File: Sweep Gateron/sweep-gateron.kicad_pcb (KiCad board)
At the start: 2 copper layers, 229.5 x 95.2 mm, 61 parts, among them J1 AudioJack4dpb, J2 AudioJack4dpb, SW10 SW_Push, SW11 SW_Push, SW11_r1 SW_Push, SW12 SW_Push, SW12_r1 SW_Push, SW13_r1 SW_Push, SW14 SW_Push, SW15 SW_Push, SW15_r1 SW_Push, SW16 SW_Push, SW16_r1 SW_Push, SW17 SW_Push, SW17_r1 SW_Push, SW18 SW_Push, SW18_r1 SW_Push, SW2 SW_Push, SW2 SW_SPDT, SW20 SW_Push, SW21 SW_Push, SW2_r1 SW_Push, SW3 SW_Push, SW3_r1 SW_Push, SW4 SW_Push, SW4_r1 SW_Push, SW5 SW_Push, SW5_r1 SW_Push, SW6 SW_Push, SW6_r1 SW_Push, SW7_r1 SW_Push, SW8 SW_Push, SW8_r1 SW_Push, SW9 SW_Push, SW9_r1 SW_Push, U1 ProMicro-kbd, U2 ProMicro-kbd

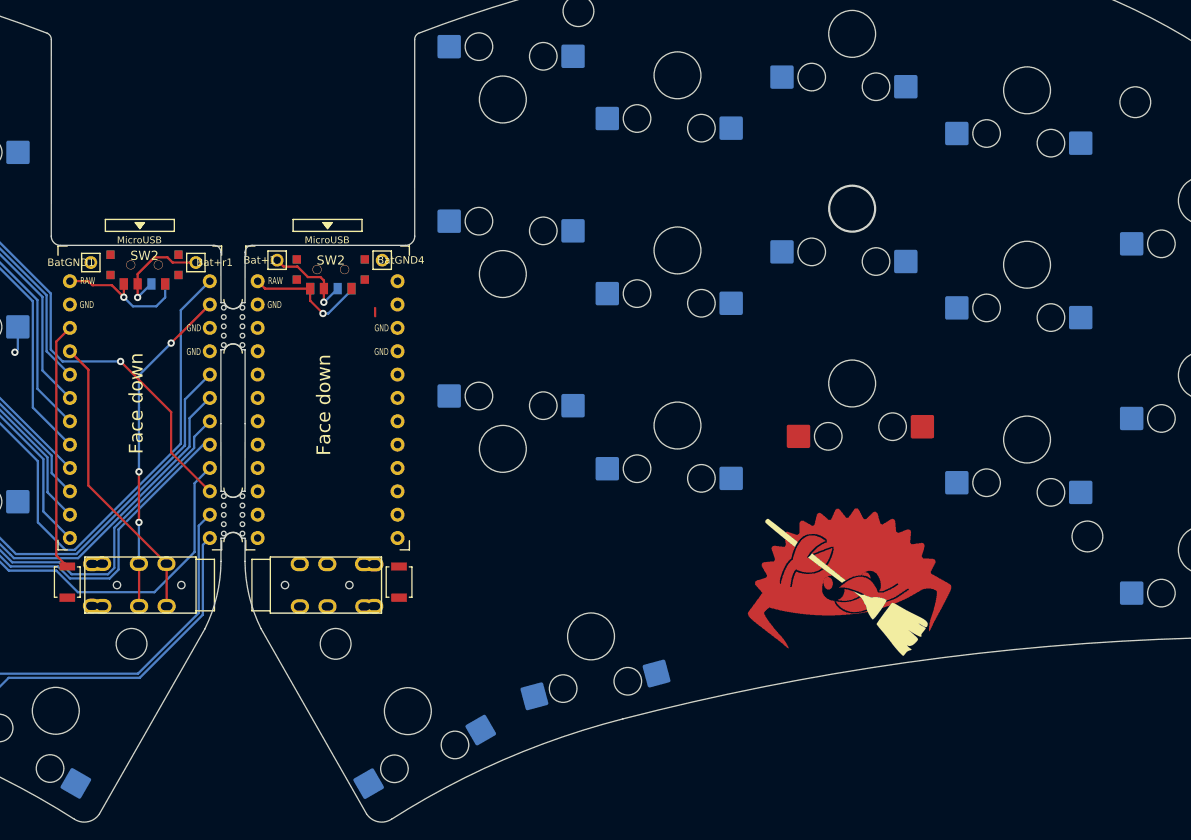
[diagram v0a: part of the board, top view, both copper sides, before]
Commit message: Routed the right side pcb
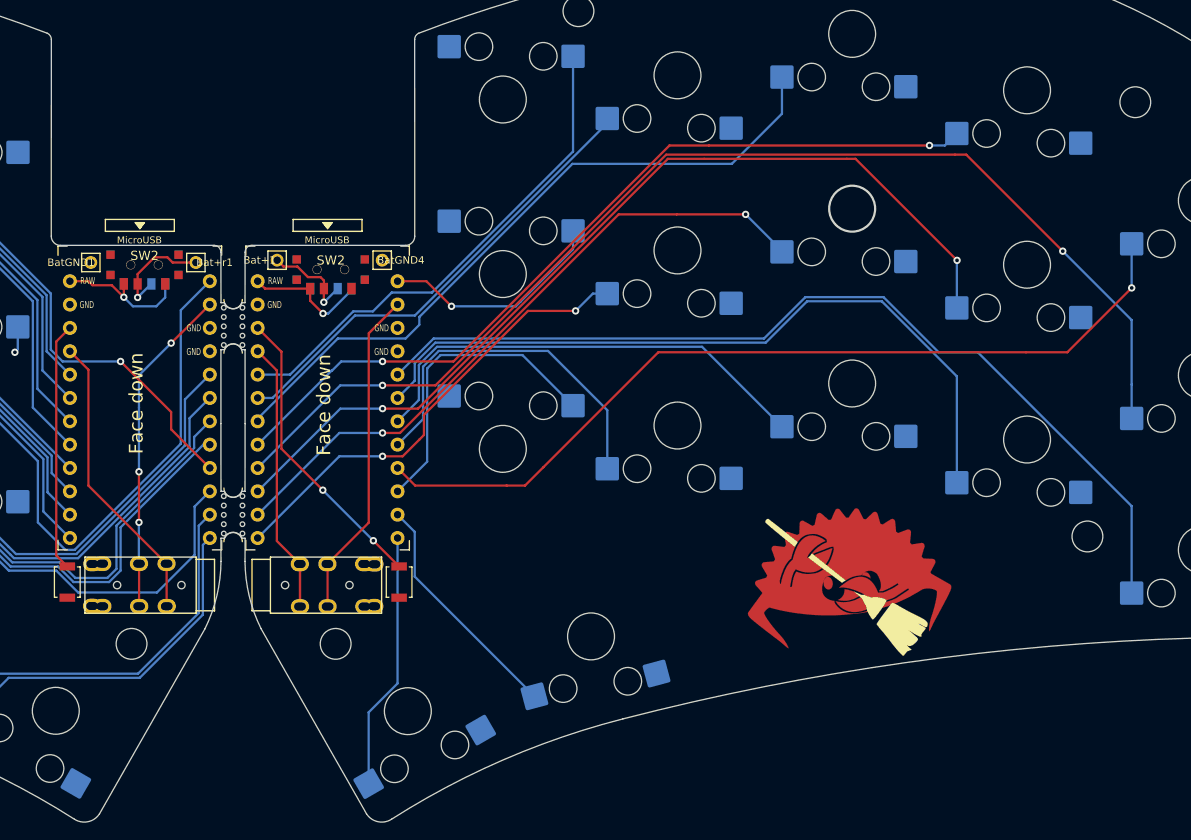
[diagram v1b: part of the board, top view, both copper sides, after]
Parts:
- SW14_r1: renamed from SW15_r1; moved to B.Cu
- moved SW20 21.5 mm to (189.2, 124.4), turned to -165 degrees
- moved SW21 21.5 mm to (169.3, 132.5), turned to -150 degrees
- moved SW20 21.3 mm to (111.3, 124.3), turned to 165 degrees
- moved SW21 21.3 mm to (130.9, 132.5), turned to 150 degrees
- turned SW14_r1 to 180 degrees
- renumbered SW11_r1 to SW10_r1, SW12_r1 to SW11_r1, SW13_r1 to SW12_r1, SW18_r1 to SW13_r1, SW16_r1 to SW15_r1, SW17_r1 to SW16_r1
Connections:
- SW10_r1 pad 1: Switch10_r -> Switch9_r
- SW11_r1 pad 1: Switch11_r -> Switch10_r
- SW12_r1 pad 1: Switch12_r -> Switch11_r
- SW13_r1 pad 1: Switch17_r -> Switch12_r
- SW14_r1 pad 1: Switch14_r -> Switch13_r
- SW15_r1 pad 1: Switch15_r -> Switch14_r
- SW16_r1 pad 1: Switch16_r -> Switch15_r
- SW20 pad 1: Switch16 -> Switch16_r
- SW21 pad 1: Switch17 -> Switch17_r
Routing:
- net Switch6_r: track 0.00 -> 127.4 mm, vias 0 -> 2
- net Switch11_r: track 0.00 -> 102.2 mm
- net Switch7_r: track 0.00 -> 100.8 mm, vias 0 -> 2
- net Switch1_r: track 0.00 -> 94.4 mm, vias 0 -> 1
- net Switch2_r: track 0.72 -> 90.1 mm, vias 0 -> 2
- net Switch12_r: track 0.00 -> 81.3 mm
- net Switch3_r: track 0.00 -> 75.6 mm
- net Switch8_r: track 0.00 -> 72.3 mm, vias 0 -> 2
- net Switch5_r: track 0.89 -> 54.7 mm
- net Switch13_r: track 0.00 -> 51.0 mm
- net Switch4_r: track 0.00 -> 50.9 mm
- net Switch9_r: track 0.00 -> 50.3 mm, vias 0 -> 2
- net Switch14_r: track 0.00 -> 39.4 mm
- net Switch18_r: track 0.00 -> 36.0 mm
- net Switch15_r: track 0.00 -> 33.5 mm
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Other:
- board text removed: "${REFERENCE}"
